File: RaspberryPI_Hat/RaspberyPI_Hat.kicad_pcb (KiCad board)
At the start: 2 copper layers, 65 x 56 mm, 45 parts, among them Q1 BC817, Q2 BC817, Q3 BC817, SW1 SW_PUSH, U1 CAT24C32WI-GT3

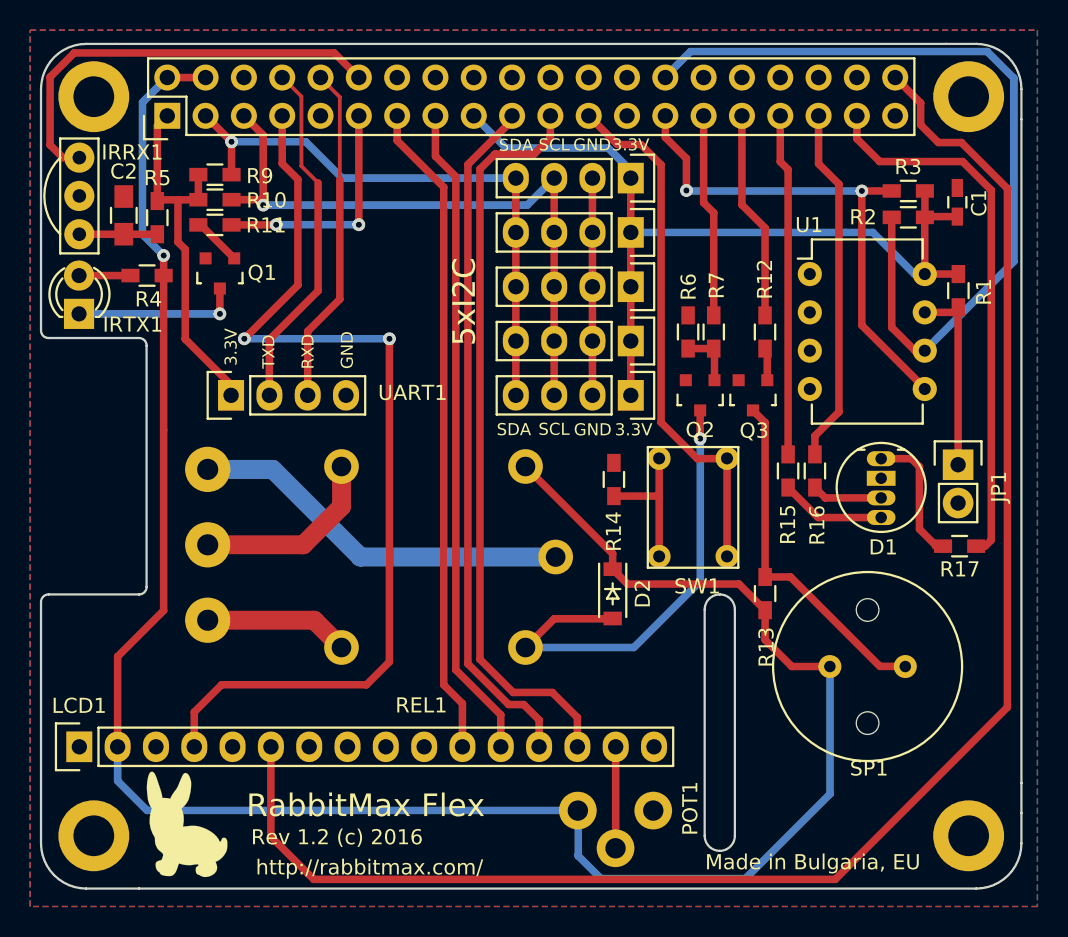
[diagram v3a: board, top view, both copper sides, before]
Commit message: Buton drill holes sizes, buzzer, moved POT1
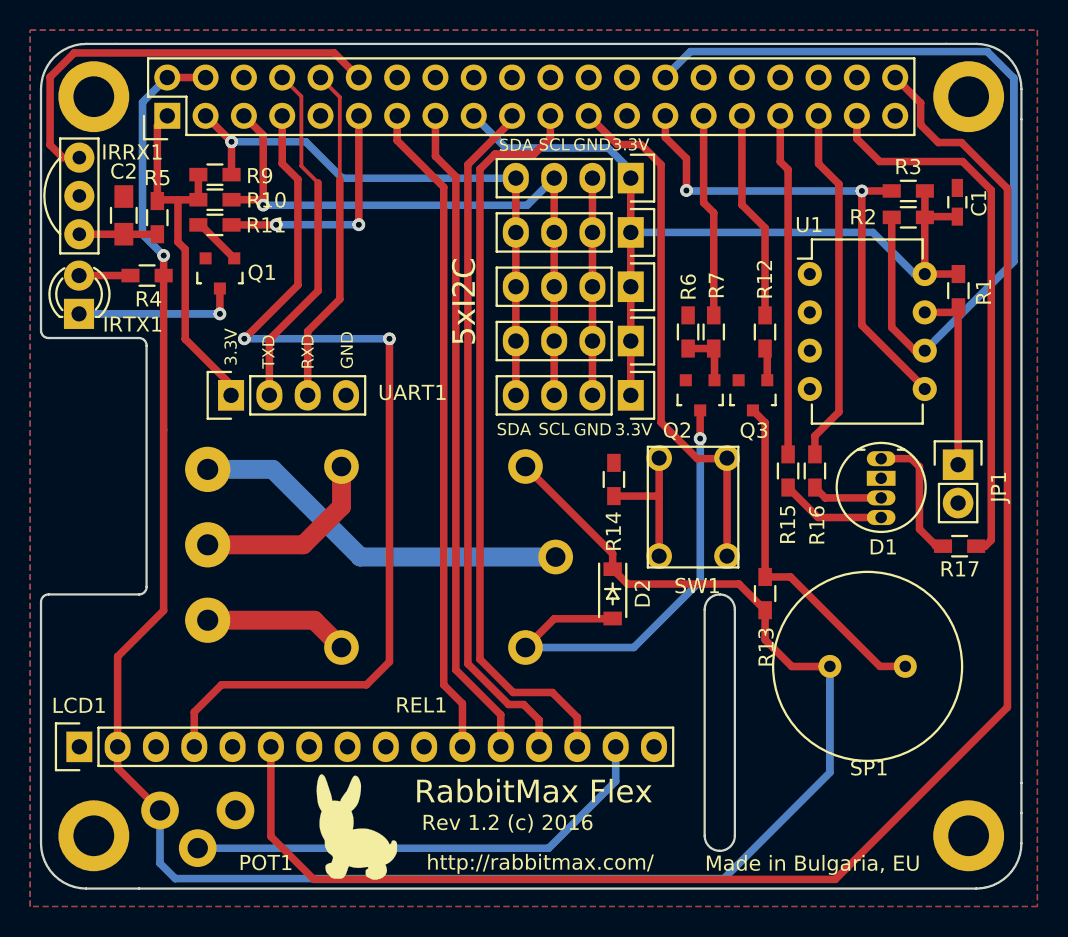
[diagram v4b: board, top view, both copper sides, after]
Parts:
- moved POT1 27.7 mm to (105.9, 119.4)
- moved G*** 11.3 mm to (118.9, 120.5)
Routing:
- net Net-(LCD1-Pad15): track 6.72 -> 31.8 mm
- net +5V: track 141.6 -> 140.6 mm
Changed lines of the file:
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@@
     (links 111)
     (no_connects 1)
-    (area 97.924999 68.524999 163.075001 124.675001)
+    (area 86.242429 56.842428 174.757572 125.790001)
     (thickness 1.6)
     (drawings 45)
@@
     (tags SOT-23)
     (attr smd)
-    (fp_text reference Q2 (at 0 -2.3 360) (layer F.SilkS)
+    (fp_text reference Q2 (at 1.51 -2.34 360) (layer F.SilkS)
       (effects (font (size 1 1) (thickness 0.15)))
     )
@@
   )
   (module myfootprint:POT_VERT (layer F.Cu)
-    (at 133.59 119.43 90)
-    (fp_text reference POT1 (at 0.14622 7.45538 90) (layer F.SilkS)
+    (at 105.89 119.42 90)
+    (fp_text reference POT1 (at -3.49 7.02 180) (layer F.SilkS)
       (effects (font (size 1 1) (thickness 0.15)))
     )
@@
   )
   (module myfootprint:logo (layer F.Cu)
-    (at 107.65 120.35)
+    (at 118.91 120.53)
     (fp_text reference G*** (at 0 0) (layer F.SilkS) hide
       (effects (font (thickness 0.3)))
@@
       (xy -2.418658 -3.439868) (xy -2.366727 -3.483398) (xy -2.310234 -3.499233) (xy -2.249089 -3.487442)) (layer F.SilkS) (width 0.01))
   )
-  (module myfootprint:TACT_SW_6 (layer F.Cu)
-    (at 138.98 96.08)
-    (fp_text reference SW1 (at 2.54 8.49) (layer F.SilkS)
-      (effects (font (size 1 1) (thickness 0.15)))
-    )
-    (fp_text value SW_PUSH (at 2.26 -2.29) (layer F.Fab)
-      (effects (font (size 1 1) (thickness 0.15)))
-    )
-    (fp_line (start -0.75 -0.75) (end 5.25 -0.75) (layer F.SilkS) (width 0.15))
-    (fp_line (start 5.25 -0.75) (end 5.25 7.25) (layer F.SilkS) (width 0.15))
-    (fp_line (start 5.25 7.25) (end -0.75 7.25) (layer F.SilkS) (width 0.15))
-    (fp_line (start -0.75 7.25) (end -0.75 -0.75) (layer F.SilkS) (width 0.15))
-    (pad 1 thru_hole circle (at 0 0) (size 1.524 1.524) (drill 0.8) (layers *.Cu *.Mask F.SilkS)
-      (net 17 "Net-(R14-Pad1)"))
-    (pad 2 thru_hole circle (at 4.5 0) (size 1.524 1.524) (drill 0.8) (layers *.Cu *.Mask F.SilkS)
-      (net 29 "Net-(RASP_CONN1-Pad23)"))
-    (pad 1 thru_hole circle (at 0 6.5) (size 1.524 1.524) (drill 0.8) (layers *.Cu *.Mask F.SilkS)
-      (net 17 "Net-(R14-Pad1)"))
-    (pad 2 thru_hole circle (at 4.5 6.5) (size 1.524 1.524) (drill 0.8) (layers *.Cu *.Mask F.SilkS)
-      (net 29 "Net-(RASP_CONN1-Pad23)"))
-  )
   (module myfootprint:MURATA_PKM13 (layer F.Cu)
-    (at 150.3 109.88)
+    (at 150.3 109.87)
     (fp_text reference SP1 (at 2.6 6.76) (layer F.SilkS)
       (effects (font (size 1 1) (thickness 0.15)))
@@
     (pad 2 thru_hole circle (at 5 0) (size 1.524 1.524) (drill 0.762) (layers *.Cu *.Mask F.SilkS)
       (net 16 "Net-(Q3-Pad3)"))
-    (pad "" np_thru_hole circle (at 2.5 -3.75) (size 1.5 1.5) (drill 1.5) (layers *.Cu *.Mask F.SilkS))
-    (pad "" np_thru_hole circle (at 2.5 3.75) (size 1.5 1.5) (drill 1.5) (layers *.Cu *.Mask F.SilkS))
-  )
-  (gr_text http://rabbitmax.com/ (at 119.775 123.2) (layer F.SilkS)
+  )
+  (module myfootprint:TACT_SW_6 (layer F.Cu)
+    (at 138.98 96.06)
+    (fp_text reference SW1 (at 2.54 8.49) (layer F.SilkS)
+      (effects (font (size 1 1) (thickness 0.15)))
+    )
+    (fp_text value SW_PUSH (at 2.26 -2.29) (layer F.Fab)
+      (effects (font (size 1 1) (thickness 0.15)))
+    )
+    (fp_line (start -0.75 -0.75) (end 5.25 -0.75) (layer F.SilkS) (width 0.15))
+    (fp_line (start 5.25 -0.75) (end 5.25 7.25) (layer F.SilkS) (width 0.15))
+    (fp_line (start 5.25 7.25) (end -0.75 7.25) (layer F.SilkS) (width 0.15))
+    (fp_line (start -0.75 7.25) (end -0.75 -0.75) (layer F.SilkS) (width 0.15))
+    (pad 1 thru_hole circle (at 0 0) (size 1.7 1.7) (drill 1) (layers *.Cu *.Mask F.SilkS)
+      (net 17 "Net-(R14-Pad1)"))
+    (pad 2 thru_hole circle (at 4.5 0) (size 1.7 1.7) (drill 1) (layers *.Cu *.Mask F.SilkS)
+      (net 29 "Net-(RASP_CONN1-Pad23)"))
+    (pad 1 thru_hole circle (at 0 6.5) (size 1.7 1.7) (drill 1) (layers *.Cu *.Mask F.SilkS)
+      (net 17 "Net-(R14-Pad1)"))
+    (pad 2 thru_hole circle (at 4.5 6.5) (size 1.7 1.7) (drill 1) (layers *.Cu *.Mask F.SilkS)
+      (net 29 "Net-(RASP_CONN1-Pad23)"))
+  )
+  (gr_text http://rabbitmax.com/ (at 131.09 122.88) (layer F.SilkS)
     (effects (font (size 1 1) (thickness 0.25)))
   )
-  (gr_text "Rev 1.2 (c) 2016" (at 117.625 121.2) (layer F.SilkS)
+  (gr_text "Rev 1.2 (c) 2016" (at 128.94 120.25) (layer F.SilkS)
     (effects (font (size 1 1) (thickness 0.25)))
   )
-  (gr_text "RabbitMax Flex\n" (at 119.525 119.1) (layer F.SilkS)
+  (gr_text "RabbitMax Flex\n" (at 130.65 118.19) (layer F.SilkS)
     (effects (font (size 1.5 1.5) (thickness 0.3)))
   )
-  (gr_text "Made in Bulgaria, EU" (at 149.1683 122.85502) (layer F.SilkS)
+  (gr_text "Made in Bulgaria, EU" (at 149.16 122.95) (layer F.SilkS)
     (effects (font (size 1 1) (thickness 0.15)))
   )
@@
   (segment (start 105.71 81.22) (end 103.49 81.22) (width 0.5) (layer F.Cu) (net 3) (status 30))
   (segment (start 103.49 81.22) (end 100.54 81.22) (width 0.5) (layer F.Cu) (net 3) (status 30))
-  (segment (start 133.61 119.42) (end 105.03 119.42) (width 0.5) (layer B.Cu) (net 4))
-  (segment (start 103.08 117.47) (end 103.08 115.202) (width 0.5) (layer B.Cu) (net 4))
-  (segment (start 105.03 119.42) (end 103.08 117.47) (width 0.5) (layer B.Cu) (net 4))
-  (segment (start 133.61 119.42) (end 133.61 122.43) (width 0.5) (layer B.Cu) (net 4))
-  (segment (start 150.31 118.33) (end 150.31 109.88) (width 0.5) (layer B.Cu) (net 4))
-  (segment (start 144.7 123.94) (end 150.31 118.33) (width 0.5) (layer B.Cu) (net 4))
-  (segment (start 135.12 123.94) (end 144.7 123.94) (width 0.5) (layer B.Cu) (net 4))
-  (segment (start 133.61 122.43) (end 135.12 123.94) (width 0.5) (layer B.Cu) (net 4))
+  (segment (start 105.89 119.42) (end 105.89 122.93) (width 0.5) (layer B.Cu) (net 4))
+  (segment (start 150.3 116.91) (end 150.3 109.87) (width 0.5) (layer B.Cu) (net 4))
+  (segment (start 143.27 123.94) (end 150.3 116.91) (width 0.5) (layer B.Cu) (net 4))
+  (segment (start 106.9 123.94) (end 143.27 123.94) (width 0.5) (layer B.Cu) (net 4))
+  (segment (start 105.89 122.93) (end 106.9 123.94) (width 0.5) (layer B.Cu) (net 4))
+  (segment (start 103.08 115.202) (end 103.08 116.61) (width 0.5) (layer F.Cu) (net 4))
+  (segment (start 103.08 116.61) (end 105.89 119.42) (width 0.5) (layer F.Cu) (net 4))
   (segment (start 146.006 106.142) (end 146.002 106.142) (width 0.5) (layer F.Cu) (net 4))
   (segment (start 146.002 106.142) (end 144.27 104.41) (width 0.5) (layer F.Cu) (net 4))
@@
   (segment (start 109.05 106.81) (end 116.11 106.81) (width 1.254) (layer F.Cu) (net 51))
   (segment (start 116.11 106.81) (end 117.92 108.62) (width 1.254) (layer F.Cu) (net 51))
-  (segment (start 136.1 115.202) (end 136.1 121.91) (width 0.5) (layer F.Cu) (net 52))
-  (segment (start 136.1 121.91) (end 136.11 121.92) (width 0.5) (layer F.Cu) (net 52))
+  (segment (start 108.39 121.92) (end 131.66 121.92) (width 0.5) (layer B.Cu) (net 52))
+  (segment (start 136.1 117.48) (end 136.1 115.202) (width 0.5) (layer B.Cu) (net 52))
+  (segment (start 131.66 121.92) (end 136.1 117.48) (width 0.5) (layer B.Cu) (net 52))
   (zone (net 1) (net_name GND) (layer F.Cu) (hatch edge 0.508)
     (connect_pads (clearance 0.254))

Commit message: POT1 connected to PIN3 of LCD, added R8, for LCD backlight current limit.
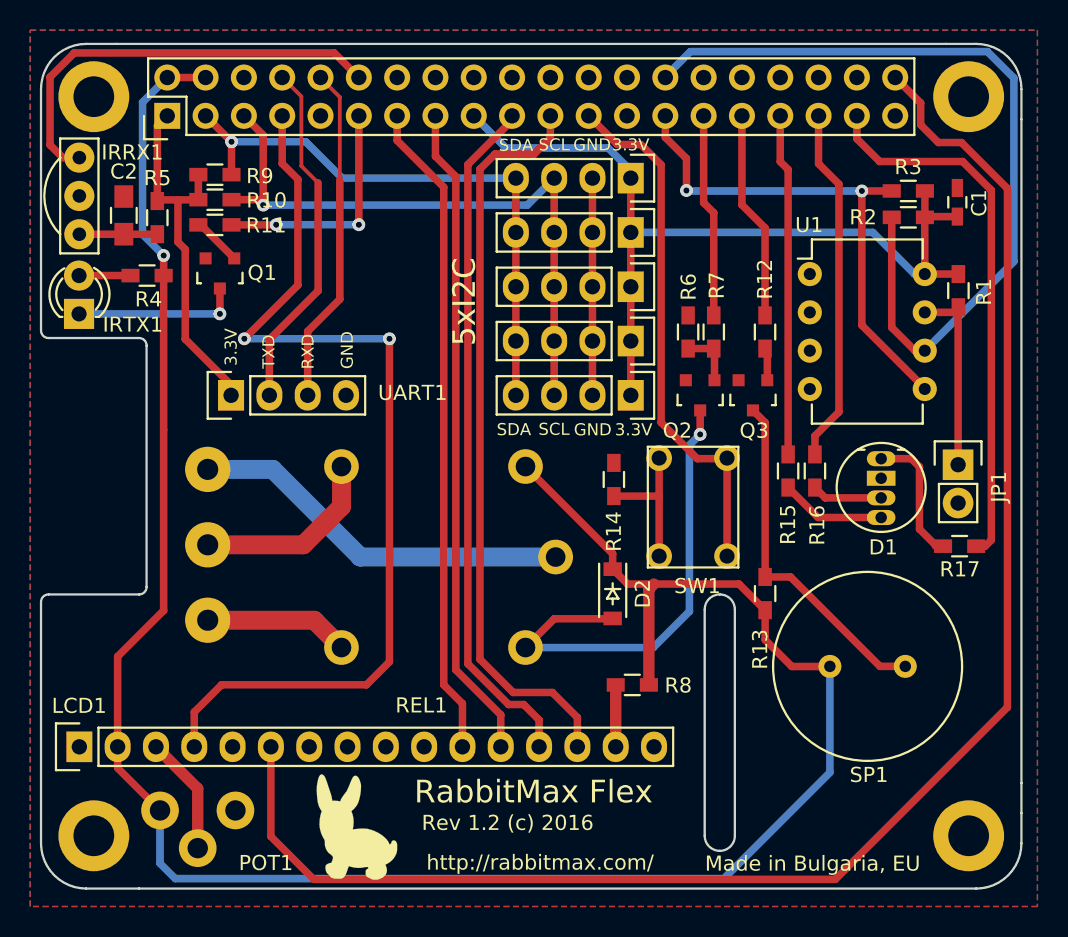
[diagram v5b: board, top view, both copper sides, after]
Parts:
- added R8: 330, Resistors_SMD:R_0603_HandSoldering, F.Cu at (137.2, 111.1)
- R10, R2, R3, R9: value 3.9K -> 4.7K
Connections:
- LCD1 pad 3: GND -> Net-(LCD1-Pad3)
- POT1 pad 2: Net-(LCD1-Pad15) -> Net-(LCD1-Pad3)
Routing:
- net Net-(LCD1-Pad15): track 31.8 -> 4.10 mm
- net Net-(LCD1-Pad3): track 0.00 -> 7.87 mm
- net +5V: track 140.6 -> 147.4 mm
- net Net-(D2-Pad2): track 31.3 -> 32.1 mm
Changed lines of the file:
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@@
-(kicad_pcb (version 4) (host pcbnew 4.0.2+e4-6225~38~ubuntu15.10.1-stable)
+(kicad_pcb (version 4) (host pcbnew 4.0.4+e1-6308~48~ubuntu16.04.1-stable)
   (general
-    (links 111)
+    (links 112)
     (no_connects 1)
-    (area 86.242429 56.842428 174.757572 125.790001)
+    (area 97.924999 68.524999 163.075001 124.675001)
     (thickness 1.6)
     (drawings 45)
-    (tracks 261)
+    (tracks 265)
     (zones 0)
-    (modules 45)
-    (nets 53)
+    (modules 46)
+    (nets 54)
   )
   (page A4)
@@
   )
   (setup
-    (last_trace_width 0.5)
+    (last_trace_width 0.754)
     (user_trace_width 0.254)
     (user_trace_width 0.5)
@@
   (net 51 "Net-(KL1-Pad3)")
   (net 52 "Net-(LCD1-Pad15)")
+  (net 53 "Net-(LCD1-Pad3)")
   (net_class Default "This is the default net class."
     (clearance 0.254)
@@
     (add_net "Net-(LCD1-Pad10)")
     (add_net "Net-(LCD1-Pad15)")
+    (add_net "Net-(LCD1-Pad3)")
     (add_net "Net-(LCD1-Pad7)")
     (add_net "Net-(LCD1-Pad8)")
@@
       (effects (font (size 1 1) (thickness 0.15)))
     )
-    (fp_text value 3.9K (at 0 1.9 180) (layer F.Fab)
+    (fp_text value 4.7K (at 0 1.9 180) (layer F.Fab)
       (effects (font (size 1 1) (thickness 0.15)))
     )
@@
       (effects (font (size 1 1) (thickness 0.15)))
     )
-    (fp_text value 3.9K (at 0 1.9 180) (layer F.Fab)
+    (fp_text value 4.7K (at 0 1.9 180) (layer F.Fab)
       (effects (font (size 1 1) (thickness 0.15)))
     )
@@
       (effects (font (size 1 1) (thickness 0.15)))
     )
-    (fp_text value 3.9K (at 0 1.9) (layer F.Fab)
+    (fp_text value 4.7K (at 0 1.9) (layer F.Fab)
       (effects (font (size 1 1) (thickness 0.15)))
     )
@@
       (effects (font (size 1 1) (thickness 0.15)))
     )
-    (fp_text value 3.9K (at 0 1.9) (layer F.Fab)
+    (fp_text value 4.7K (at 0 1.9) (layer F.Fab)
       (effects (font (size 1 1) (thickness 0.15)))
     )
@@
     (tags "resistor 0603")
     (attr smd)
-    (fp_text reference R13 (at -3.558 0.094 90) (layer F.SilkS)
+    (fp_text reference R13 (at -3.698 -0.326 90) (layer F.SilkS)
       (effects (font (size 1 1) (thickness 0.15)))
     )
@@
       (net 4 +5V))
     (pad 3 thru_hole oval (at 0 5.08 90) (size 2.032 1.7272) (drill 1.016) (layers *.Cu *.Mask F.SilkS)
-      (net 1 GND))
+      (net 53 "Net-(LCD1-Pad3)"))
     (pad 4 thru_hole oval (at 0 7.62 90) (size 2.032 1.7272) (drill 1.016) (layers *.Cu *.Mask F.SilkS)
       (net 12 /RS))
@@
       (net 4 +5V))
     (pad 2 thru_hole circle (at -2.5 2.5 90) (size 2.5 2.5) (drill 1.35) (layers *.Cu *.Mask F.SilkS)
-      (net 52 "Net-(LCD1-Pad15)"))
+      (net 53 "Net-(LCD1-Pad3)"))
     (pad 3 thru_hole circle (at 0 5 90) (size 2.5 2.5) (drill 1.35) (layers *.Cu *.Mask F.SilkS)
       (net 1 GND))
@@
   (module myfootprint:MURATA_PKM13 (layer F.Cu)
     (at 150.3 109.87)
-    (fp_text reference SP1 (at 2.6 6.76) (layer F.SilkS)
+    (fp_text reference SP1 (at 2.59 7.2) (layer F.SilkS)
       (effects (font (size 1 1) (thickness 0.15)))
     )
@@
     (pad 2 thru_hole circle (at 4.5 6.5) (size 1.7 1.7) (drill 1) (layers *.Cu *.Mask F.SilkS)
       (net 29 "Net-(RASP_CONN1-Pad23)"))
+  )
+  (module Resistors_SMD:R_0603_HandSoldering (layer F.Cu)
+    (at 137.2 111.1)
+    (descr "Resistor SMD 0603, hand soldering")
+    (tags "resistor 0603")
+    (attr smd)
+    (fp_text reference R8 (at 3.05 0.04) (layer F.SilkS)
+      (effects (font (size 1 1) (thickness 0.15)))
+    )
+    (fp_text value 330 (at 0 1.9) (layer F.Fab)
+      (effects (font (size 1 1) (thickness 0.15)))
+    )
+    (fp_line (start -2 -0.8) (end 2 -0.8) (layer F.CrtYd) (width 0.05))
+    (fp_line (start -2 0.8) (end 2 0.8) (layer F.CrtYd) (width 0.05))
+    (fp_line (start -2 -0.8) (end -2 0.8) (layer F.CrtYd) (width 0.05))
+    (fp_line (start 2 -0.8) (end 2 0.8) (layer F.CrtYd) (width 0.05))
+    (fp_line (start 0.5 0.675) (end -0.5 0.675) (layer F.SilkS) (width 0.15))
+    (fp_line (start -0.5 -0.675) (end 0.5 -0.675) (layer F.SilkS) (width 0.15))
+    (pad 1 smd rect (at -1.1 0) (size 1.2 0.9) (layers F.Cu F.Paste F.Mask)
+      (net 52 "Net-(LCD1-Pad15)"))
+    (pad 2 smd rect (at 1.1 0) (size 1.2 0.9) (layers F.Cu F.Paste F.Mask)
+      (net 4 +5V))
+    (model Resistors_SMD.3dshapes/R_0603_HandSoldering.wrl
+      (at (xyz 0 0 0))
+      (scale (xyz 1 1 1))
+      (rotate (xyz 0 0 0))
+    )
   )
   (gr_text http://rabbitmax.com/ (at 131.09 122.88) (layer F.SilkS)
@@
   (segment (start 105.71 81.22) (end 103.49 81.22) (width 0.5) (layer F.Cu) (net 3) (status 30))
   (segment (start 103.49 81.22) (end 100.54 81.22) (width 0.5) (layer F.Cu) (net 3) (status 30))
+  (segment (start 138.3 111.1) (end 138.3 104.74) (width 0.754) (layer F.Cu) (net 4))
+  (segment (start 138.3 104.74) (end 138.63 104.41) (width 0.754) (layer F.Cu) (net 4))
   (segment (start 105.89 119.42) (end 105.89 122.93) (width 0.5) (layer B.Cu) (net 4))
   (segment (start 150.3 116.91) (end 150.3 109.87) (width 0.5) (layer B.Cu) (net 4))
@@
   (segment (start 146.002 106.142) (end 144.27 104.41) (width 0.5) (layer F.Cu) (net 4))
   (segment (start 136.885 104.41) (end 135.9 103.425) (width 0.5) (layer F.Cu) (net 4))
-  (segment (start 144.27 104.41) (end 136.885 104.41) (width 0.5) (layer F.Cu) (net 4))
+  (segment (start 144.27 104.41) (end 140.78 104.41) (width 0.5) (layer F.Cu) (net 4))
+  (segment (start 140.78 104.41) (end 138.63 104.41) (width 0.5) (layer F.Cu) (net 4))
+  (segment (start 138.63 104.41) (end 136.885 104.41) (width 0.5) (layer F.Cu) (net 4))
   (segment (start 135.9 103.425) (end 135.9 102.4) (width 0.5) (layer F.Cu) (net 4))
   (segment (start 135.9 102.4) (end 130.12 96.62) (width 0.5) (layer F.Cu) (net 4))
@@
   (segment (start 147.778 109.878) (end 150.324 109.878) (width 0.5) (layer F.Cu) (net 4))
   (segment (start 146.006 108.106) (end 147.778 109.878) (width 0.5) (layer F.Cu) (net 4))
-  (segment (start 141.7 92.89822) (end 141.7 94.77) (width 0.5) (layer F.Cu) (net 5))
-  (segment (start 137.3 108.62) (end 130.12 108.62) (width 0.5) (layer B.Cu) (net 5))
-  (segment (start 141.71 104.21) (end 137.3 108.62) (width 0.5) (layer B.Cu) (net 5))
-  (segment (start 141.71 94.78) (end 141.71 104.21) (width 0.5) (layer B.Cu) (net 5))
-  (segment (start 141.7 94.77) (end 141.71 94.78) (width 0.5) (layer B.Cu) (net 5))
-  (via (at 141.7 94.77) (size 0.85) (drill 0.4) (layers F.Cu B.Cu) (net 5))
+  (segment (start 141.7 92.89822) (end 141.7 94.49) (width 0.5) (layer F.Cu) (net 5))
+  (segment (start 138.59 108.62) (end 130.12 108.62) (width 0.5) (layer B.Cu) (net 5))
+  (segment (start 140.99 106.22) (end 138.59 108.62) (width 0.5) (layer B.Cu) (net 5))
+  (segment (start 140.99 95.2) (end 140.99 106.22) (width 0.5) (layer B.Cu) (net 5))
+  (segment (start 141.7 94.49) (end 140.99 95.2) (width 0.5) (layer B.Cu) (net 5))
+  (via (at 141.7 94.49) (size 0.85) (drill 0.4) (layers F.Cu B.Cu) (net 5))
   (segment (start 135.92 106.715) (end 132.025 106.715) (width 0.5) (layer F.Cu) (net 5))
   (segment (start 132.025 106.715) (end 130.12 108.62) (width 0.5) (layer F.Cu) (net 5))
@@
   (segment (start 109.05 106.81) (end 116.11 106.81) (width 1.254) (layer F.Cu) (net 51))
   (segment (start 116.11 106.81) (end 117.92 108.62) (width 1.254) (layer F.Cu) (net 51))
-  (segment (start 108.39 121.92) (end 131.66 121.92) (width 0.5) (layer B.Cu) (net 52))
-  (segment (start 136.1 117.48) (end 136.1 115.202) (width 0.5) (layer B.Cu) (net 52))
-  (segment (start 131.66 121.92) (end 136.1 117.48) (width 0.5) (layer B.Cu) (net 52))
+  (segment (start 136.1 115.202) (end 136.1 111.1) (width 0.754) (layer F.Cu) (net 52))
+  (segment (start 108.39 121.92) (end 108.39 117.972) (width 0.754) (layer F.Cu) (net 53))
+  (segment (start 108.39 117.972) (end 105.62 115.202) (width 0.754) (layer F.Cu) (net 53))
   (zone (net 1) (net_name GND) (layer F.Cu) (hatch edge 0.508)
     (connect_pads (clearance 0.254))
@@
     (polygon
       (pts
-        (xy 164.06 125.79) (xy 97.28 125.79) (xy 97.28 67.69) (xy 164.06 67.69) (xy 164.06 125.79)
+        (xy 164.06 125.79) (xy 97.28 125.79) (xy 97.28 67.69) (xy 164.06 67.69)
       )
     )
@@
     (polygon
       (pts
-        (xy 164.06 125.79) (xy 97.28 125.79) (xy 97.28 67.69) (xy 164.06 67.69) (xy 164.06 125.79)
+        (xy 164.06 125.79) (xy 97.28 125.79) (xy 97.28 67.69) (xy 164.06 67.69)
       )
     )
@@
     (polygon
       (pts
-        (xy 134.86 113.32) (xy 105 113.32) (xy 105 93.71) (xy 134.86 93.71) (xy 134.86 113.32)
+        (xy 134.86 113.32) (xy 105 113.32) (xy 105 93.71) (xy 134.86 93.71)
       )
     )
@@
     (polygon
       (pts
-        (xy 134.86 113.32) (xy 105 113.32) (xy 105 93.71) (xy 134.86 93.71) (xy 134.86 113.32)
+        (xy 134.86 113.32) (xy 105 113.32) (xy 105 93.71) (xy 134.86 93.71)
       )
     )
